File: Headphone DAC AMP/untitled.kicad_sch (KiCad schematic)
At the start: 18 parts, among them U10 TLV71x_WSON-6, U11 ADP2108AUJ-1.8, U9 NUP2202

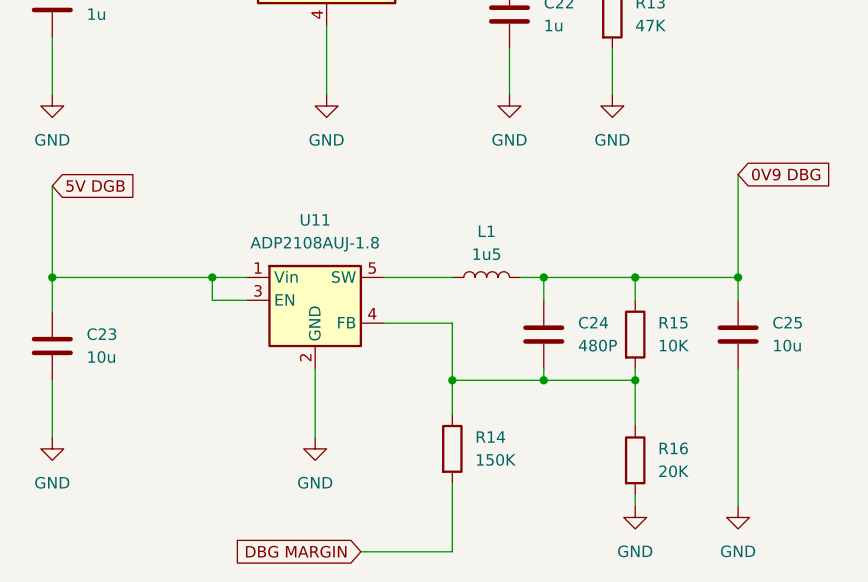
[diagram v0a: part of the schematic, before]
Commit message: addad crystal placeholder
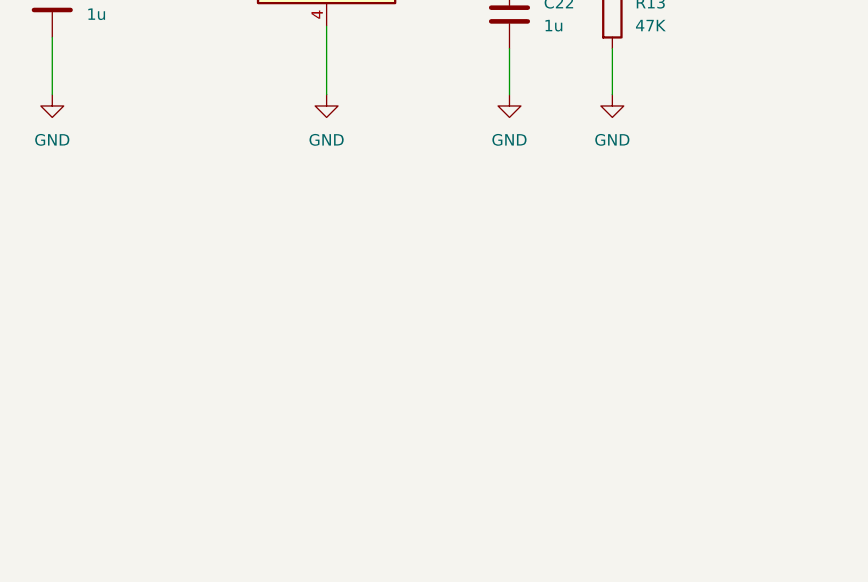
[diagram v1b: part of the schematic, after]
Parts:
- removed C23, C25: 10u, symbol Device:C
- removed C24: 480P, symbol Device:C
- removed L1: 1u5, symbol Device:L
- removed R14: 150K, symbol Device:R
- removed R15: 10K, symbol Device:R
- removed R16: 20K, symbol Device:R
- removed U11: ADP2108AUJ-1.8, Package_TO_SOT_SMD:TSOT-23-5, symbol Regulator_Switching:ADP2108AUJ-1.8

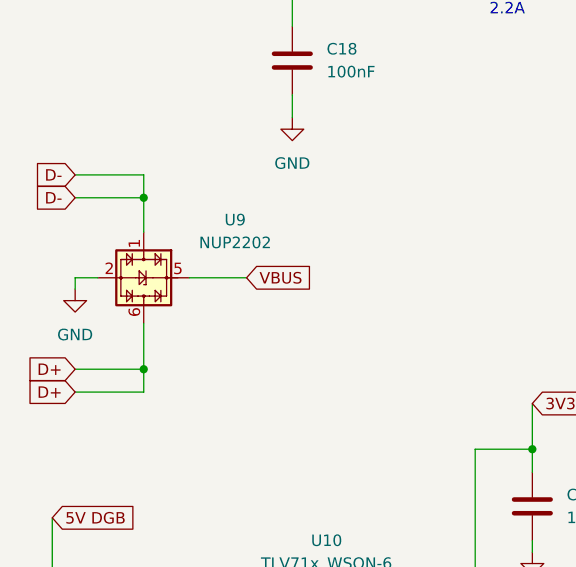
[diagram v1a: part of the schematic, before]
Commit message: Added crystals
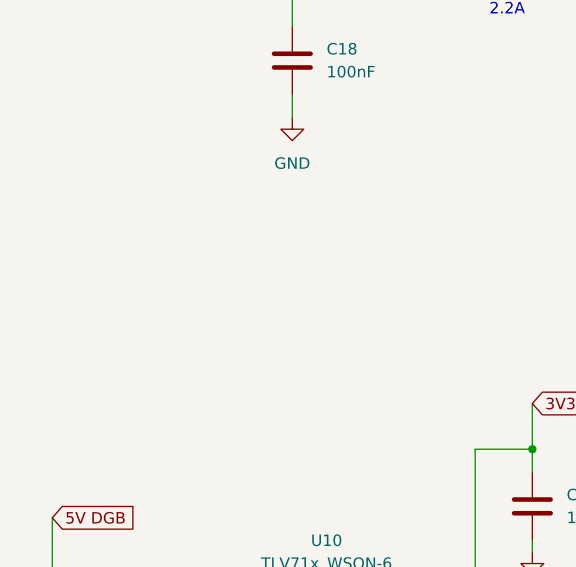
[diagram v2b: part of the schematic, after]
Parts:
- removed U9: NUP2202, Package_TO_SOT_SMD:SOT-363_SC-70-6, symbol Power_Protection:NUP2202

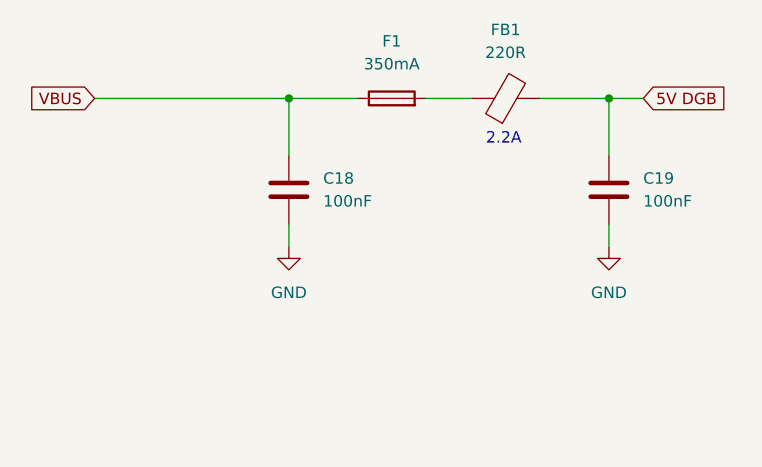
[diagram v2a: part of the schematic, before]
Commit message: Began connecting Root page
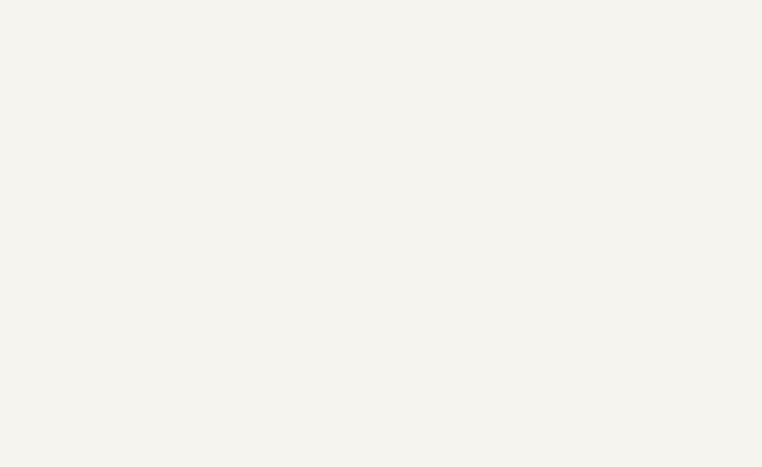
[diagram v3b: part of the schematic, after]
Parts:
- removed C18, C19: 100nF, symbol Device:C
- removed F1: 350mA, symbol Device:Fuse
- removed FB1: 220R, symbol Device:FerriteBead
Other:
- note removed: "2.2A"

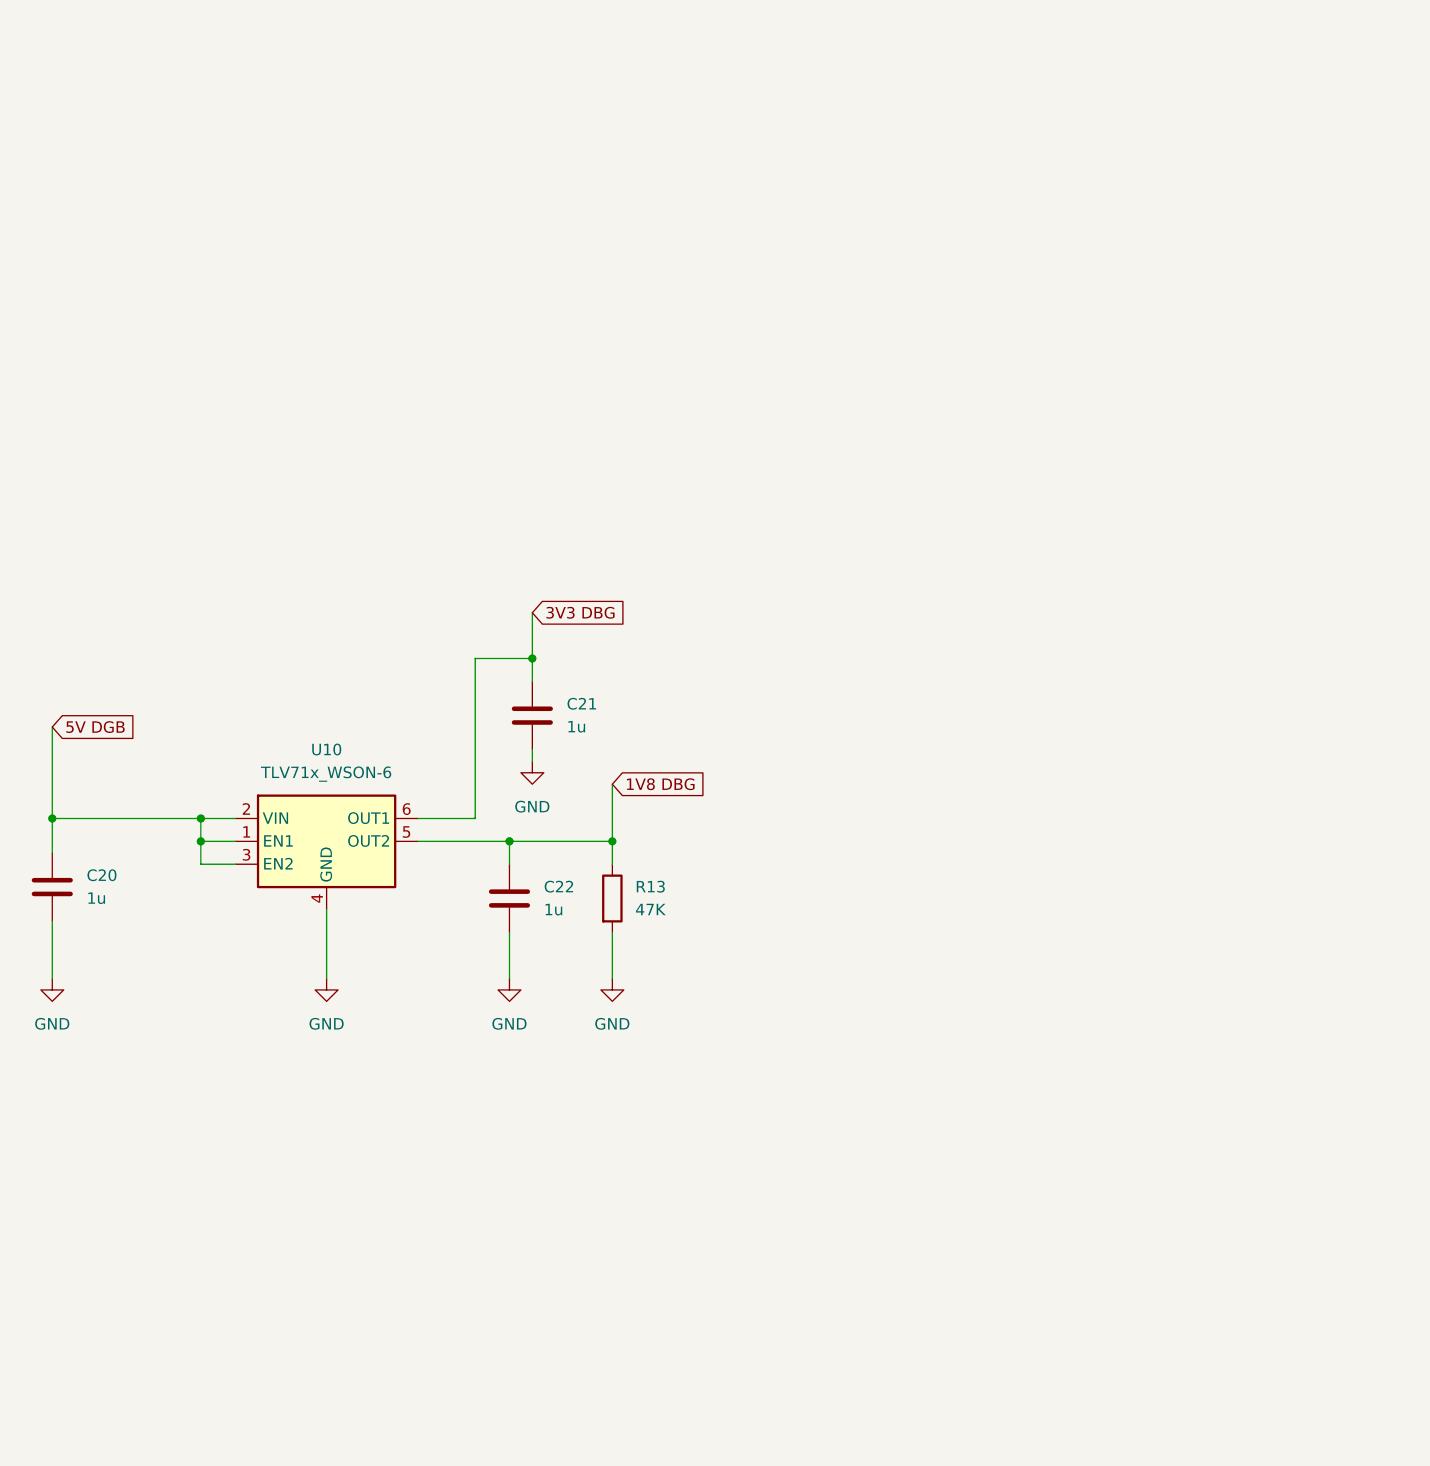
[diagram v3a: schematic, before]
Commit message: added boost for 12v rail
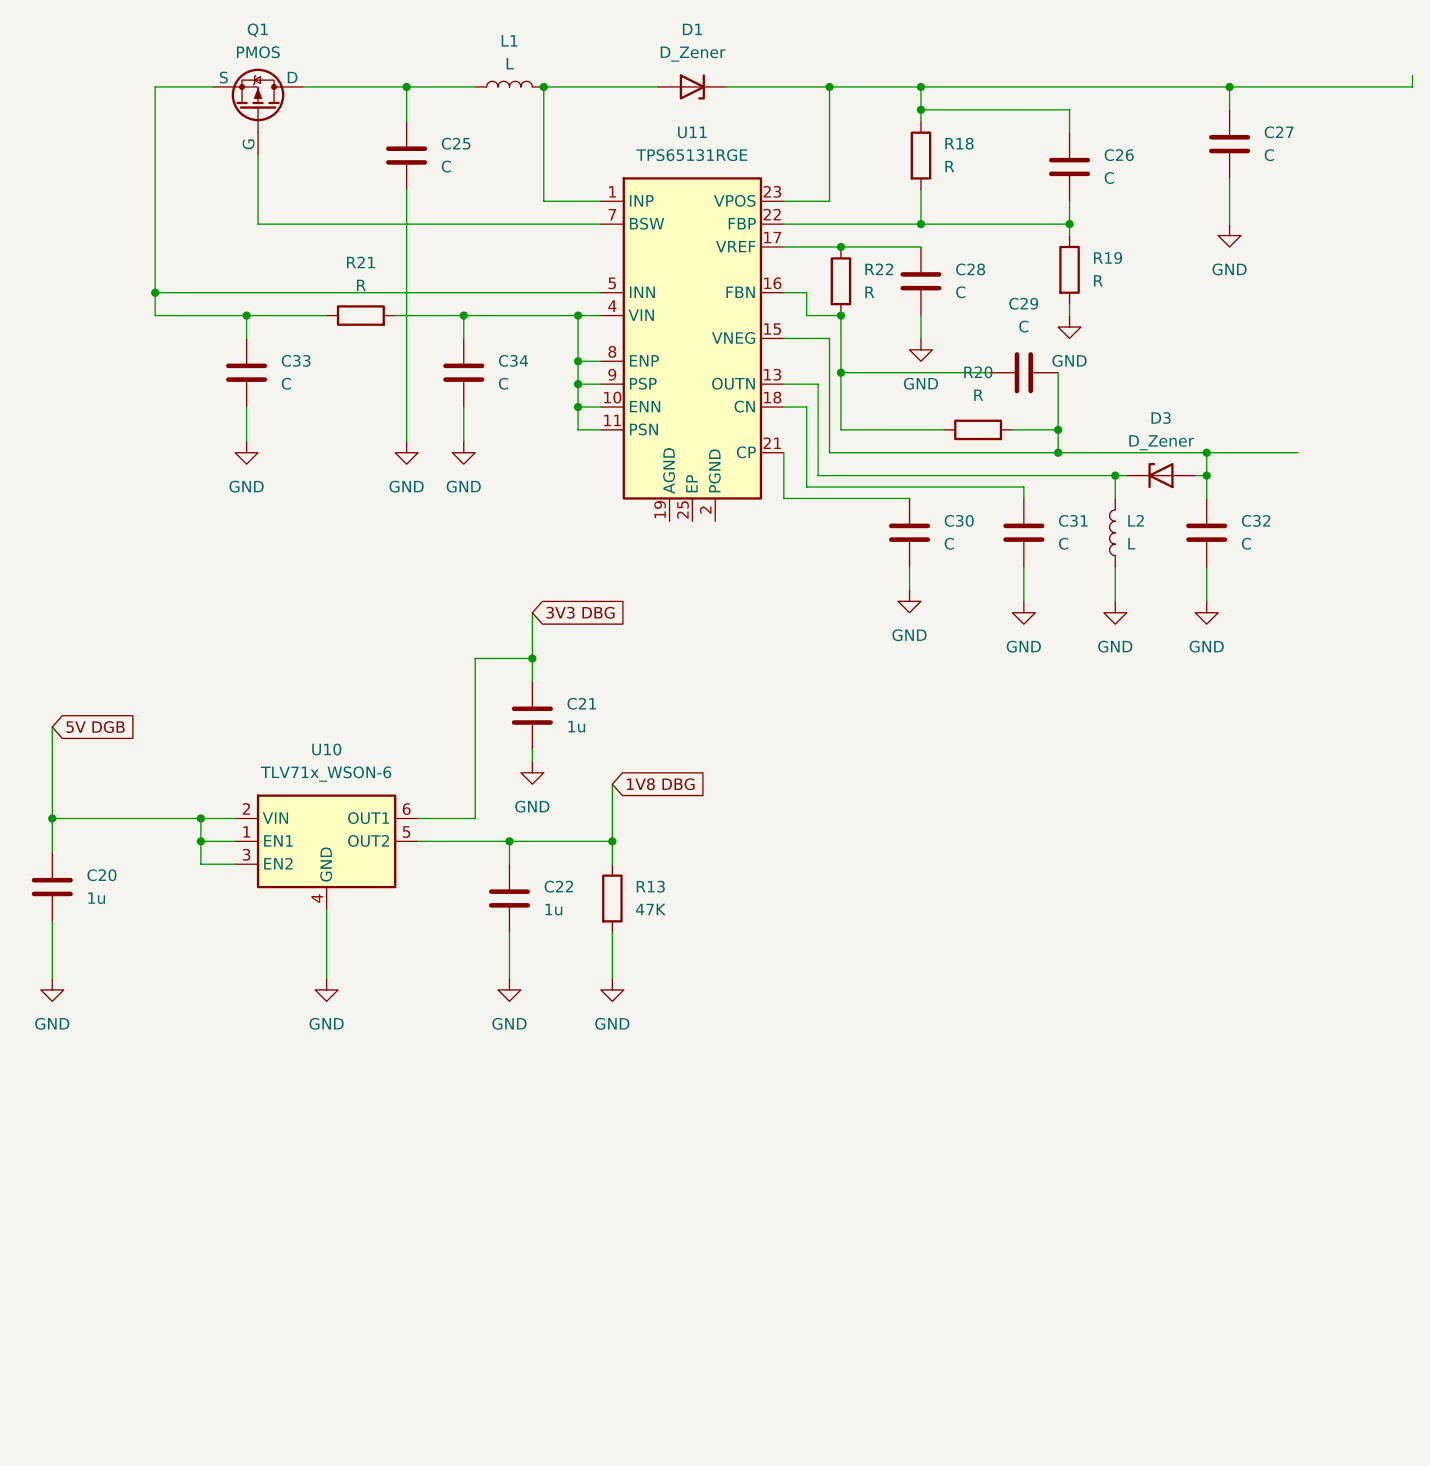
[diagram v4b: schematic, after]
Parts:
- added C25, C26, C27, C28, C29, C30, C31, C32, C33, C34: C, symbol Device:C
- added D1, D3: D_Zener, symbol Device:D_Zener
- added L1, L2: L, symbol Device:L
- added Q1: PMOS, symbol Simulation_SPICE:PMOS
- added R18, R19, R20, R21, R22: R, symbol Device:R
- added U11: TPS65131RGE, Package_DFN_QFN:VQFN-24-1EP_4x4mm_P0.5mm_EP2.45x2.45mm_ThermalVias, symbol Regulator_Switching:TPS65131RGE
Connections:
- net GND: now also C25.2, C27.2, C28.2, C30.1, C31.1, C32.1, C33.2, C34.2, L2.1, R19.2
- new net: C25.1, L1.1, Q1.1 (D)
- new net: Q1.2 (G), U11.7 (BSW)
- new net: C33.1, Q1.3 (S), R21.1, U11.5 (INN), U11.6 (INN)
- new net: C26.1, C27.1, D1.1 (K), R18.1, U11.23 (VPOS)
- new net: C26.2, R18.2, R19.1, U11.22 (FBP)
- new net: C31.2, U11.18 (CN)
- new net: C29.1, R20.1, R22.2, U11.16 (FBN)
- new net: C29.2, C32.2, D3.2 (A), R20.2, U11.15 (VNEG)
- new net: C28.1, R22.1, U11.17 (VREF)
- new net: C34.1, R21.2, U11.10 (ENN), U11.11 (PSN), U11.4 (VIN), U11.8 (ENP), U11.9 (PSP)
- new net: D1.2 (A), L1.2, U11.1 (INP), U11.24 (INP)
- new net: D3.1 (K), L2.2, U11.13 (OUTN), U11.14 (OUTN)
- new net: U11.2 (PGND), U11.3 (PGND)
- new net: C30.2, U11.21 (CP)
